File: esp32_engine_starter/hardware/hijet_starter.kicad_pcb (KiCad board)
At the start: 2 copper layers, 100 x 82 mm, 37 parts, among them J1 12V IN, J2 REMOTE OUT, J3 AUX IN, J4 I2C, J5 ESP32 J1, J6 ESP32 J3, U1 OKI-78SR-5/1.5-W36-C, U2 PC817C, U3 PC817C, U4 PC817C, U5 PC817C, U6 PC817C, U7 PC817C

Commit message: Drop the engine starter from the plan; relabel PCB outputs
The engine starter will not be installed. Output 1 is now the vehicle
door-lock signal for BLE walk-away locking and outputs 2-4 are generic
isolated outputs. Silkscreen, BOM and READMEs updated; DRC still clean.

Co-Authored-By: Claude Opus 5.5 <noreply@anthropic.com>
Claude-Session: https://claude.ai/code/session_011cXkDUypHbxixpJEznYmeT
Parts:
- J2: value REMOTE OUT -> OUT
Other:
- board text added: "+ OUT2 -"
- board text added: "+ OUT3 -"
- board text added: "+ OUT4 -"
- board text removed: "+ START -"
- board text removed: "+ STOP -"
- board text removed: "+ UNLK -"

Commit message: PCB: retarget to the 30-pin ESP32 DevKit V1 (HW-394)
The ESP32 board actually bought is the 30-pin DevKit V1 clone, not the
38-pin DevKitC. Switch to 1x15 sockets with its pin order (VIN row left,
3V3 row right, 25.4 mm row pitch), move the antenna keepout and C3,
rename the board, and update the docs. DRC: 0 violations, 0 unconnected.

Co-Authored-By: Claude Opus 5.5 <noreply@anthropic.com>
Claude-Session: https://claude.ai/code/session_011cXkDUypHbxixpJEznYmeT
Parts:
- J5: value ESP32 J1 -> ESP32 VIN row; footprint PinSocket_1x19_P2.54mm_Vertical -> PinSocket_1x15_P2.54mm_Vertical
- J6: value ESP32 J3 -> ESP32 3V3 row; footprint PinSocket_1x19_P2.54mm_Vertical -> PinSocket_1x15_P2.54mm_Vertical
- moved C3 9.00 mm to (57.0, 47.0)
- moved J5 2.00 mm to (62.0, 10.0)
- moved J6 2.00 mm to (87.4, 10.0)
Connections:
- J5 pad 1: +3V3 -> (no net)
- J5 pad 10: G26 -> G27
- J5 pad 11: G27 -> (no net)
- J5 pad 15: (no net) -> +5V
- J5 pad 4: (no net) -> VSENSE
- J5 pad 5: VSENSE -> G35
- J5 pad 6: G35 -> G32
- J5 pad 7: G32 -> G33
- J5 pad 8: G33 -> G25
- J5 pad 9: G25 -> G26
- J6 pad 1: GND -> (no net)
- J6 pad 14: (no net) -> GND
- J6 pad 15: (no net) -> +3V3
- J6 pad 2: (no net) -> SCL
- J6 pad 3: SCL -> (no net)
- J6 pad 5: (no net) -> SDA
- J6 pad 6: SDA -> (no net)
- J6 pad 7: GND -> (no net)
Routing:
- net +3V3: track 141.0 -> 96.2 mm, vias 1 -> 0
- net +5V: track 55.2 -> 46.5 mm
- net VSENSE: track 34.3 -> 35.1 mm
- net G35: track 69.6 -> 68.9 mm
- net SCL: track 15.1 -> 15.6 mm
- net G33: track 52.9 -> 53.4 mm, vias 2 -> 1
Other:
- board text added: "ESP32 DevKit V1 (30pin) USB side"
- board text added: "HIJET MONITOR v2"
- board text removed: "ESP32-DevKitC USB side"
- board text removed: "HIJET STARTER v1"

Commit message: PCB v2: add OBD-II CAN, ACC sense, buzzer and GPS header
- MCP2562 CAN transceiver (5V VDD, 3.3V VIO) on GPIO18/19 with a CAN-H/
  CAN-L/GND terminal for the OBD-II port
- Third isolated input on GPIO36 for ACC (ignition) detection
- 5V buzzer driven by 2SC1815 from GPIO23
- UART GPS header on GPIO16/17
- Board grows to 100x92 mm; GND link for the GPS header; refdes fixes
DRC: 0 violations, 0 unconnected. Firmware pin map updated in config.h.

Co-Authored-By: Claude Opus 5.5 <noreply@anthropic.com>
Claude-Session: https://claude.ai/code/session_011cXkDUypHbxixpJEznYmeT
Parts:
- added BZ1: Buzzer 5V 12mm, Buzzer_12x9.5RM7.6, F.Cu at (68.0, 64.0)
- added C5: 0.1uF, C_Disc_D5.0mm_W2.5mm_P2.50mm, F.Cu at (61.5, 82.0)
- added C6: 0.1uF, C_Disc_D5.0mm_W2.5mm_P2.50mm, F.Cu at (78.0, 87.5)
- added D6: 1N4148, D_DO-35_SOD27_P7.62mm_Horizontal, F.Cu at (23.0, 78.5)
- added D7: 1N4148, D_DO-35_SOD27_P7.62mm_Horizontal, F.Cu at (67.0, 72.5)
- added J7: OBD-II CAN, TerminalBlock_Phoenix_PT-1,5-3-3.5-H_1x03_P3.50mm_Horizontal, F.Cu at (94.5, 82.0)
- added J8: GPS, PinHeader_1x04_P2.54mm_Vertical, F.Cu at (95.0, 36.0)
- added Q1: 2SC1815, TO-92_Inline_Wide, F.Cu at (82.0, 64.0)
- added R11: 10k, R_Axial_DIN0207_L6.3mm_D2.5mm_P10.16mm_Horizontal, F.Cu at (46.0, 70.0)
- added R12: 10k, R_Axial_DIN0207_L6.3mm_D2.5mm_P10.16mm_Horizontal, F.Cu at (50.0, 77.0)
- added R13: 1k, R_Axial_DIN0207_L6.3mm_D2.5mm_P10.16mm_Horizontal, F.Cu at (91.0, 70.0)
- added U8: PC817C, DIP-4_W7.62mm, F.Cu at (28.0, 75.0)
- added U9: MCP2562-E/P, DIP-8_W7.62mm, F.Cu at (66.0, 76.0)
- J3: value AUX IN -> IN; footprint TerminalBlock_Phoenix_PT-1,5-4-3.5-H_1x04_P3.50mm_Horizontal -> TerminalBlock_Phoenix_PT-1,5-6-3.5-H_1x06_P3.50mm_Horizontal
- R9: value 10k -> 2.2k
- moved R9 30.5 mm to (14.0, 75.0), turned to 0 degrees
- moved H3 10.0 mm to (3.50, 88.5)
- moved H4 10.0 mm to (96.5, 88.5)
- moved R10 8.06 mm to (42.0, 63.0)
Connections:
- J5 pad 2: (no net) -> G36
- J6 pad 1: (no net) -> G23
- J6 pad 10: (no net) -> G16
- J6 pad 6: (no net) -> G19
- J6 pad 7: (no net) -> G18
- J6 pad 9: (no net) -> G17
- R10 pad 1: G35 -> G33
- R9 pad 1: G33 -> IN3P
- R9 pad 2: +3V3 -> IN3A
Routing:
- net G36: track 0.00 -> 91.2 mm, vias 0 -> 1
- net G19: track 0.00 -> 69.8 mm, vias 0 -> 1
- net G18: track 0.00 -> 59.8 mm, vias 0 -> 1
- net G23: track 0.00 -> 55.9 mm
- net +3V3: track 96.2 -> 149.0 mm
- net +5V: track 46.5 -> 91.0 mm
- net IN3N: track 0.00 -> 24.2 mm
- net CANH: track 0.00 -> 22.4 mm
- net CANL: track 0.00 -> 22.0 mm
- net BZN: track 0.00 -> 19.0 mm
- net G17: track 0.00 -> 17.7 mm
- net G16: track 0.00 -> 13.9 mm
- net GND: track 0.00 -> 12.1 mm, vias 0 -> 1
- net G33: track 53.4 -> 63.0 mm
- net IN3P: track 0.00 -> 8.50 mm
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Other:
- board size 100 x 82 mm -> 100 x 92 mm
- board text added: "- ACC +"
- board text added: "CAN H"
- board text added: "CAN L"
- board text added: "GPS RX"
- board text added: "GPS TX"

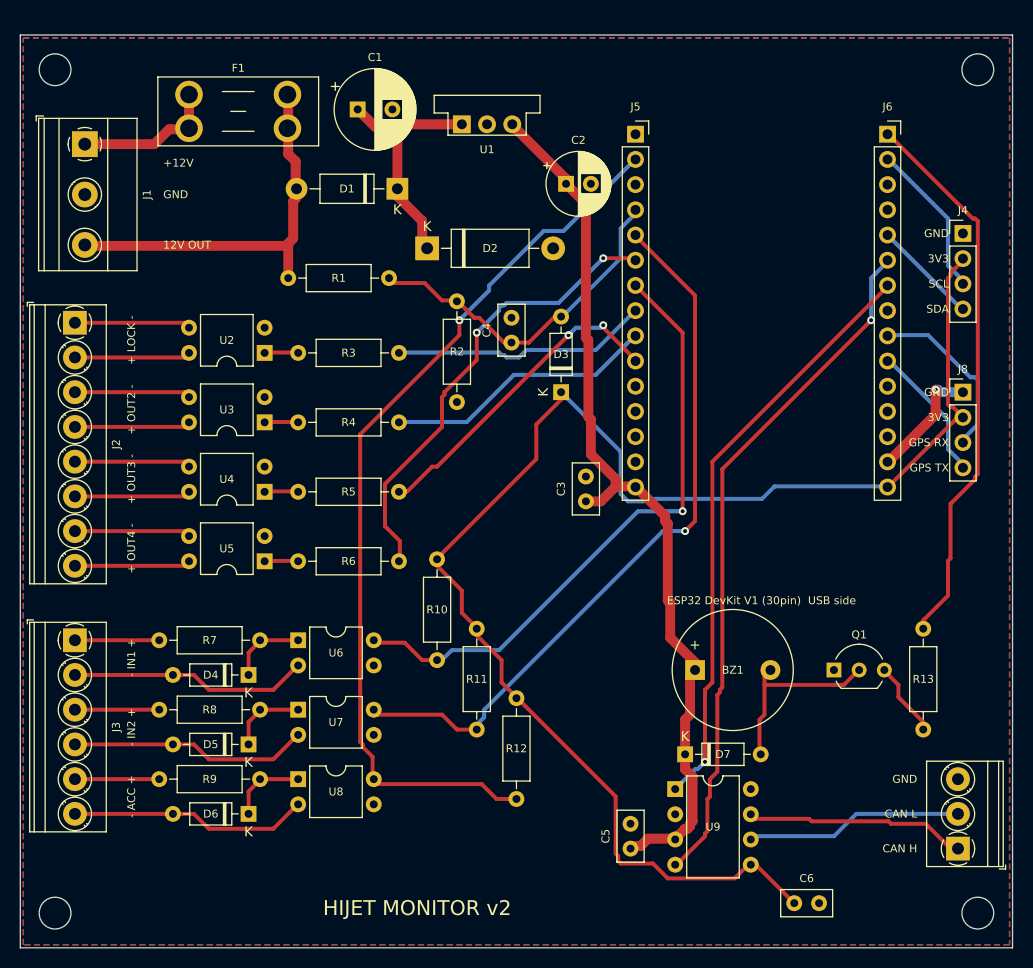
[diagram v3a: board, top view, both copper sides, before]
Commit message: PCB v3: compact 92x70 mm through-hole layout
- Low-profile parts (MCP2562, decoupling, STBY pull-up) sit under the
  socketed ESP32; resistors and diodes stand on 5.08 mm pitch
- Terminals on two edges; fuse holder replaced by a 0.5 A polyfuse
- MCP2562 STBY now pulled high (standby, bus untouched) and released by
  GPIO4; buzzer moved to GPIO13 with a 10k base pull-down
- Netlist audited against MCP2562 / OKI-78SR datasheet pinouts
DRC: 0 violations, 0 unconnected. config.h, BOM and README updated.

Co-Authored-By: Claude Opus 5.5 <noreply@anthropic.com>
Claude-Session: https://claude.ai/code/session_011cXkDUypHbxixpJEznYmeT
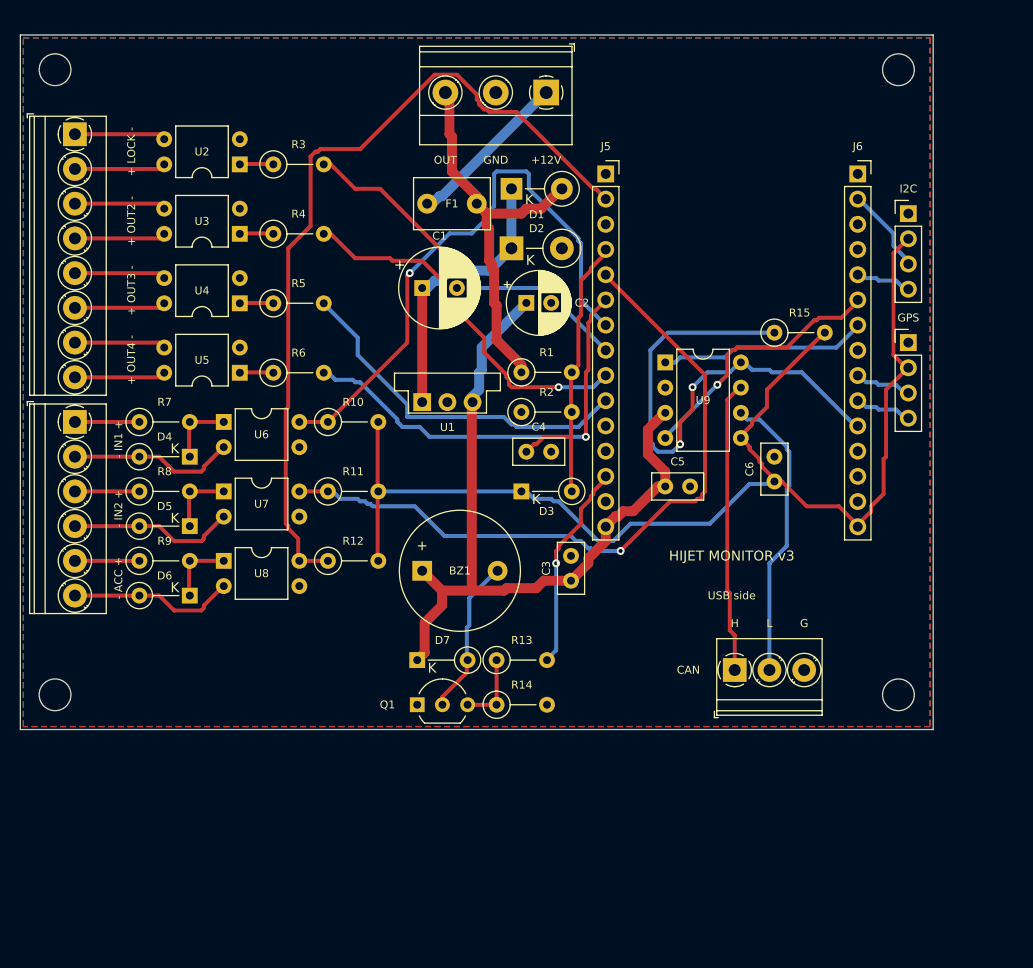
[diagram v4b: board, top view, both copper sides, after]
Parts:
- added R14: 10k, R_Axial_DIN0207_L6.3mm_D2.5mm_P5.08mm_Vertical, F.Cu at (48.0, 67.5)
- added R15: 10k, R_Axial_DIN0207_L6.3mm_D2.5mm_P5.08mm_Vertical, F.Cu at (76.0, 30.0)
- D1: footprint D_DO-41_SOD81_P10.16mm_Horizontal -> D_DO-41_SOD81_P5.08mm_Vertical_KathodeUp
- D2: footprint D_DO-15_P12.70mm_Horizontal -> D_DO-15_P5.08mm_Vertical_KathodeUp
- D3, D4, D5, D6, D7: footprint D_DO-35_SOD27_P7.62mm_Horizontal -> D_DO-35_SOD27_P5.08mm_Vertical_KathodeUp
- F1: value Mini blade 1A -> PTC 0.5A; footprint Fuseholder_Blade_Mini_Keystone_3568 -> C_Disc_D7.5mm_W5.0mm_P5.00mm
- R1, R10, R11, R12, R13, R2, R3, R4, R5, R6, R7, R8, R9: footprint R_Axial_DIN0207_L6.3mm_D2.5mm_P10.16mm_Horizontal -> R_Axial_DIN0207_L6.3mm_D2.5mm_P5.08mm_Vertical
- moved J1 46.8 mm to (53.0, 5.80), turned to 180 degrees
- moved R13 43.6 mm to (48.0, 63.0), turned to 0 degrees
- moved U9 43.0 mm to (65.0, 33.0)
- moved C6 42.5 mm to (76.0, 45.0), turned to 90 degrees
- moved Q1 42.1 mm to (40.0, 67.5)
- moved C5 36.7 mm to (65.0, 45.5), turned to 0 degrees
- moved R12 30.6 mm to (31.0, 53.0), turned to 0 degrees
- moved BZ1 29.3 mm to (40.5, 54.0)
- moved J7 28.8 mm to (72.0, 64.0), turned to 0 degrees
- moved D7 28.6 mm to (40.0, 63.0)
- moved R11 28.3 mm to (31.0, 46.0), turned to 0 degrees
- moved U1 28.3 mm to (40.5, 37.0)
- moved F1 26.4 mm to (41.0, 17.0)
- moved R10 26.4 mm to (31.0, 39.0), turned to 0 degrees
- moved R1 25.3 mm to (50.5, 34.0)
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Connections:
- J5 pad 13: (no net) -> G13
- J6 pad 1: G23 -> (no net)
- J6 pad 11: (no net) -> STBY
- R13 pad 2: G23 -> G13
- U9 pad 8: GND -> STBY
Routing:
- net G23: track 55.9 -> 0.00 mm
- net STBY: track 0.00 -> 53.1 mm, vias 0 -> 2
- net G19: track 69.8 -> 26.4 mm
- net G18: track 59.8 -> 21.1 mm, vias 1 -> 0
- net +3V3: track 149.0 -> 121.4 mm
- net G13: track 0.00 -> 21.0 mm, vias 0 -> 1
- net GND: track 12.1 -> 0.00 mm, vias 1 -> 0
- net G17: track 17.7 -> 5.72 mm
- net +5V: track 91.0 -> 79.1 mm
- net G25: track 25.9 -> 37.3 mm, vias 0 -> 1
- net G26: track 27.4 -> 37.6 mm, vias 0 -> 1
- net G16: track 13.9 -> 5.72 mm
- net CANL: track 22.0 -> 29.6 mm
- net IN3N: track 24.2 -> 16.8 mm
- net IN2N: track 24.2 -> 16.8 mm
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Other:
- board size 100 x 92 mm -> 92 x 70 mm
- board text added: "CAN"
- board text added: "G"
- board text added: "GPS"
- board text added: "H"
- board text added: "HIJET MONITOR v3"
- board text added: "I2C"
- board text added: "L"
- board text added: "OUT"
- board text added: "USB side"
- board text removed: "12V OUT"
- board text removed: "3V3"
- board text removed: "CAN H"
- board text removed: "CAN L"
- board text removed: "ESP32 DevKit V1 (30pin) USB side"
- board text removed: "GPS RX"
- board text removed: "GPS TX"
- board text removed: "HIJET MONITOR v2"
- board text removed: "SCL"
- board text removed: "SDA"

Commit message: PCB: pre-order verification suite and fixes found by it
Add automated checks to build.sh (any failure stops Gerber export):
- check_pins.py: 68 connections and 16 firmware pin numbers checked
  against an independent table from datasheets and the board photo
- check_mech.py: lead vs drill, part heights under the ESP32, USB plug
  clearance, terminal wire-entry direction, board overhang
- sim/: ngspice runs for the battery divider, opto in/out and buzzer
  driver, plus datasheet power-budget checks
- check_fab.py: drill counts/diameters match the board, layers present
Fixes from the checks: R2 22k->18k (ADC range), PTC 0.5A->0.75A (hot
derating), opto LED 470->330 ohm, R15 laid flat under the ESP32, J7
moved out of the USB plug path, silk line width 0.16 mm, T-junction
stub cleanup. BOM now lists purchase pitfalls. VERIFICATION.md added.

Co-Authored-By: Claude Opus 5.5 <noreply@anthropic.com>
Claude-Session: https://claude.ai/code/session_011cXkDUypHbxixpJEznYmeT
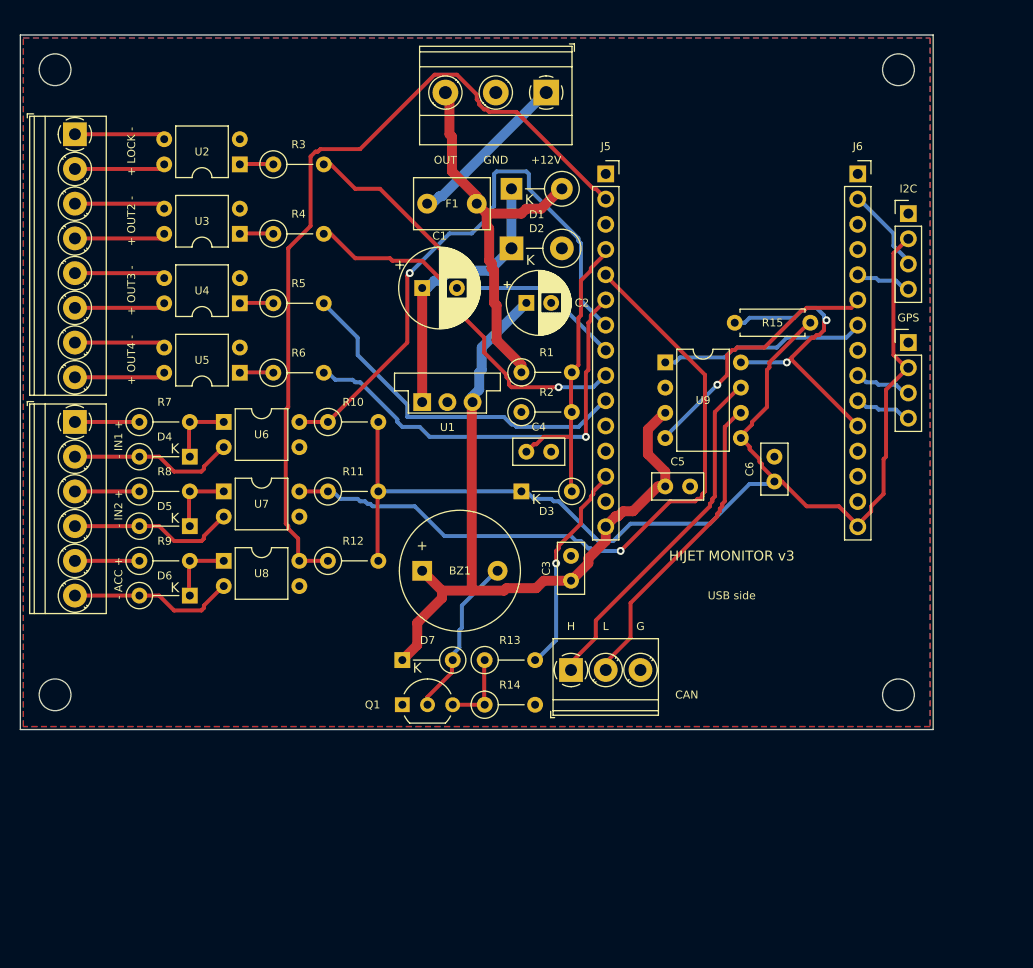
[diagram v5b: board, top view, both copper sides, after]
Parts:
- F1: value PTC 0.5A -> PTC 0.75A
- R15: footprint R_Axial_DIN0207_L6.3mm_D2.5mm_P5.08mm_Vertical -> R_Axial_DIN0207_L6.3mm_D2.5mm_P7.62mm_Horizontal
- R2: value 22k -> 18k
- R3, R4, R5, R6: value 470 -> 330
- moved J7 16.5 mm to (55.5, 64.0)
- moved R15 4.12 mm to (72.0, 29.0)
- moved D7 1.50 mm to (38.5, 63.0)
- moved Q1 1.50 mm to (38.5, 67.5)
- moved R13 1.20 mm to (46.8, 63.0)
- moved R14 1.20 mm to (46.8, 67.5)
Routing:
- net STBY: track 53.1 -> 31.3 mm
- net CANH: track 29.3 -> 35.5 mm
- net CANL: track 29.6 -> 31.6 mm
- net +5V: track 79.1 -> 79.7 mm
- net BZN: track 15.8 -> 16.4 mm

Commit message: 基板 v4：ESP32 直付け・車載保護の追加・秋月電子の部品に合わせる
- ESP32 DevKit をソケットでなく直接はんだ付けにし、下にあった U9/C5/C6/R15 を外へ移動
- 出力 4ch に双方向 TVS SMBJ45CA を追加（PC817 は VCEO 80V の X 系）
- 電源 TVS を P6KE20A に（DC-DC M78AR05-1 の入力上限 32V に対して余裕）
- 入力抵抗を 3.3k に（35V の異常電圧でも発熱が許容内）
- 端子台を 5.08mm（秋月 TB112）、ポリスイッチを RXEF090 に変更
- 部品表に秋月の商品ページ URL と買う数を追加
- check_mech/check_pins/シミュレーションを新構成に合わせ、全検証合格

Co-Authored-By: Claude Opus 5.5 <noreply@anthropic.com>
Claude-Session: https://claude.ai/code/session_011cXkDUypHbxixpJEznYmeT
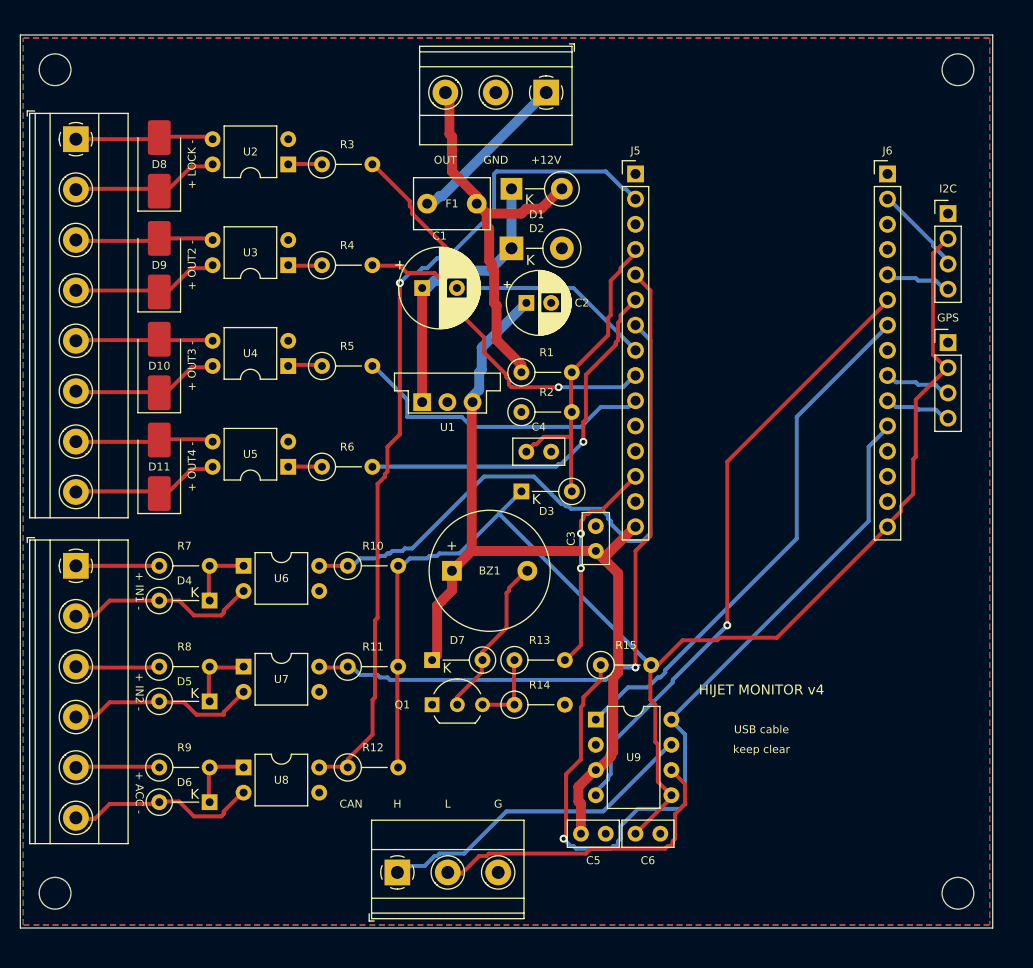
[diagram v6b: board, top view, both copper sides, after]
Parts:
- added D10: SMBJ45CA, D_SMB_Handsoldering, F.Cu at (14.0, 33.4)
- added D11: SMBJ45CA, D_SMB_Handsoldering, F.Cu at (14.0, 43.5)
- added D8: SMBJ45CA, D_SMB_Handsoldering, F.Cu at (14.0, 13.0)
- added D9: SMBJ45CA, D_SMB_Handsoldering, F.Cu at (14.0, 23.2)
- D2: value P6KE22A -> P6KE20A
- D3: value BAT85 -> BAT43
- F1: value PTC 0.75A -> PTC 0.9A
- J2: footprint TerminalBlock_Phoenix_PT-1,5-8-3.5-H_1x08_P3.50mm_Horizontal -> TerminalBlock_Phoenix_MKDS-1,5-8-5.08_1x08_P5.08mm_Horizontal
- J3: footprint TerminalBlock_Phoenix_PT-1,5-6-3.5-H_1x06_P3.50mm_Horizontal -> TerminalBlock_Phoenix_MKDS-1,5-6-5.08_1x06_P5.08mm_Horizontal
- J5, J6: footprint PinSocket_1x15_P2.54mm_Vertical -> PinHeader_1x15_P2.54mm_Vertical
- J7: footprint TerminalBlock_Phoenix_PT-1,5-3-3.5-H_1x03_P3.50mm_Horizontal -> TerminalBlock_Phoenix_MKDS-1,5-3-5.08_1x03_P5.08mm_Horizontal
- R15: footprint R_Axial_DIN0207_L6.3mm_D2.5mm_P7.62mm_Horizontal -> R_Axial_DIN0207_L6.3mm_D2.5mm_P5.08mm_Vertical
- R7, R8, R9: value 2.2k -> 3.3k
- U1: value OKI-78SR-5/1.5-W36-C -> M78AR05-1
- U2, U3, U4, U5, U6, U7, U8: value PC817C -> PC817
- moved C6 38.2 mm to (62.0, 80.5), turned to 0 degrees
- moved R15 37.0 mm to (58.5, 63.5)
- moved U9 36.7 mm to (58.0, 69.0)
- moved C5 36.0 mm to (56.5, 80.5)
- moved J7 26.9 mm to (38.0, 84.4)
- moved D6 20.9 mm to (19.1, 77.3)
- moved R12 20.9 mm to (33.0, 73.8)
- moved R9 20.9 mm to (14.0, 73.8)
- moved U8 20.9 mm to (22.5, 73.8)
- moved H4 20.9 mm to (94.5, 86.5)
- moved H3 20.0 mm to (3.50, 86.5)
- moved D5 17.8 mm to (19.1, 67.2)
- moved R11 17.8 mm to (33.0, 63.7)
- moved R8 17.8 mm to (14.0, 63.7)
- moved U7 17.8 mm to (22.5, 63.7)
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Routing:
- net STBY: track 31.3 -> 82.2 mm, vias 2 -> 1
- net G19: track 26.4 -> 62.0 mm
- net G18: track 21.1 -> 53.3 mm
- net +3V3: track 121.7 -> 139.4 mm
- net +5V: track 79.7 -> 88.4 mm
- net O2C: track 9.21 -> 15.2 mm
- net O1C: track 9.21 -> 15.2 mm
- net O4C: track 9.21 -> 15.2 mm
- net O3C: track 9.21 -> 15.1 mm
- net G27: track 36.6 -> 31.3 mm
- net G32: track 43.9 -> 38.7 mm
- net O2E: track 9.21 -> 14.2 mm
- net O4E: track 9.21 -> 14.2 mm
- net O1E: track 9.21 -> 14.2 mm
- net O3E: track 9.21 -> 14.0 mm
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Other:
- board size 92 x 70 mm -> 98 x 90 mm
- board text added: "+ ACC -"
- board text added: "+ IN1 -"
- board text added: "+ IN2 -"
- board text added: "HIJET MONITOR v4"
- board text added: "USB cable"
- board text added: "keep clear"
- board text removed: "- ACC +"
- board text removed: "- IN1 +"
- board text removed: "- IN2 +"
- board text removed: "HIJET MONITOR v3"
- board text removed: "USB side"
